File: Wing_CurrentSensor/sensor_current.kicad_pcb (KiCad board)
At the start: 2 copper layers, 50 x 50 mm, 18 parts, among them U1 TL084, U2 AD8226

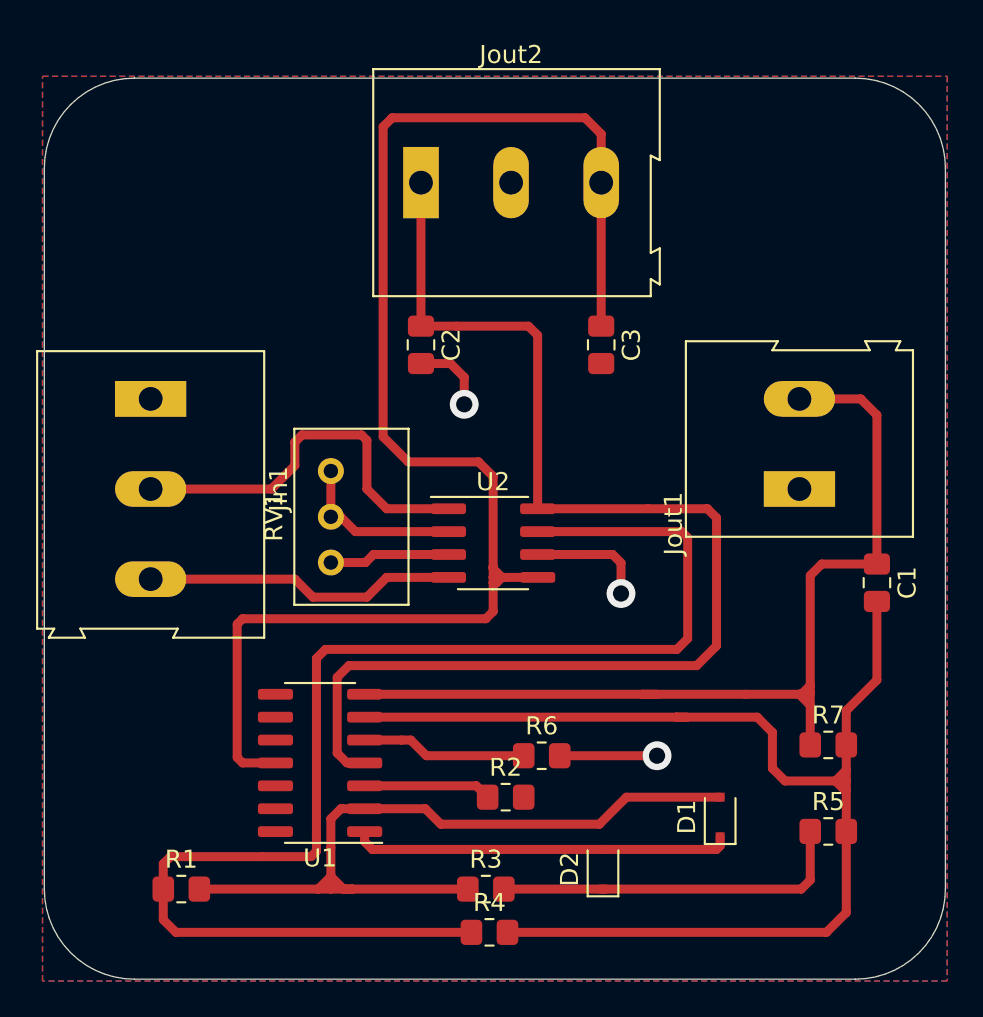
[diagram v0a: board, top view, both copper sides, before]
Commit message: AD8226 eliminated
auto_awesome
Se muestra la traducción de se reemplazo el AD8226 por un modulo del TL084, ademas se cambio el orden de los modulos, siendo estos el modulo B,C y D, se realizo nuevo esquematico y nueva PCB del circuito
Traducir se remplazo el AD8226 por un modulo del TL084, ademas se cambio el orden de los modulos, siendo estos el modulo B,C y D, se realizo nuevo esquematico y nueva PCB del circuito
174 / 5000
Resultados de traducción
The AD8226 was replaced by a TL084 module, also the order of the modules was changed, these being module B, C and D, a new schematic and new circuit PCB was made
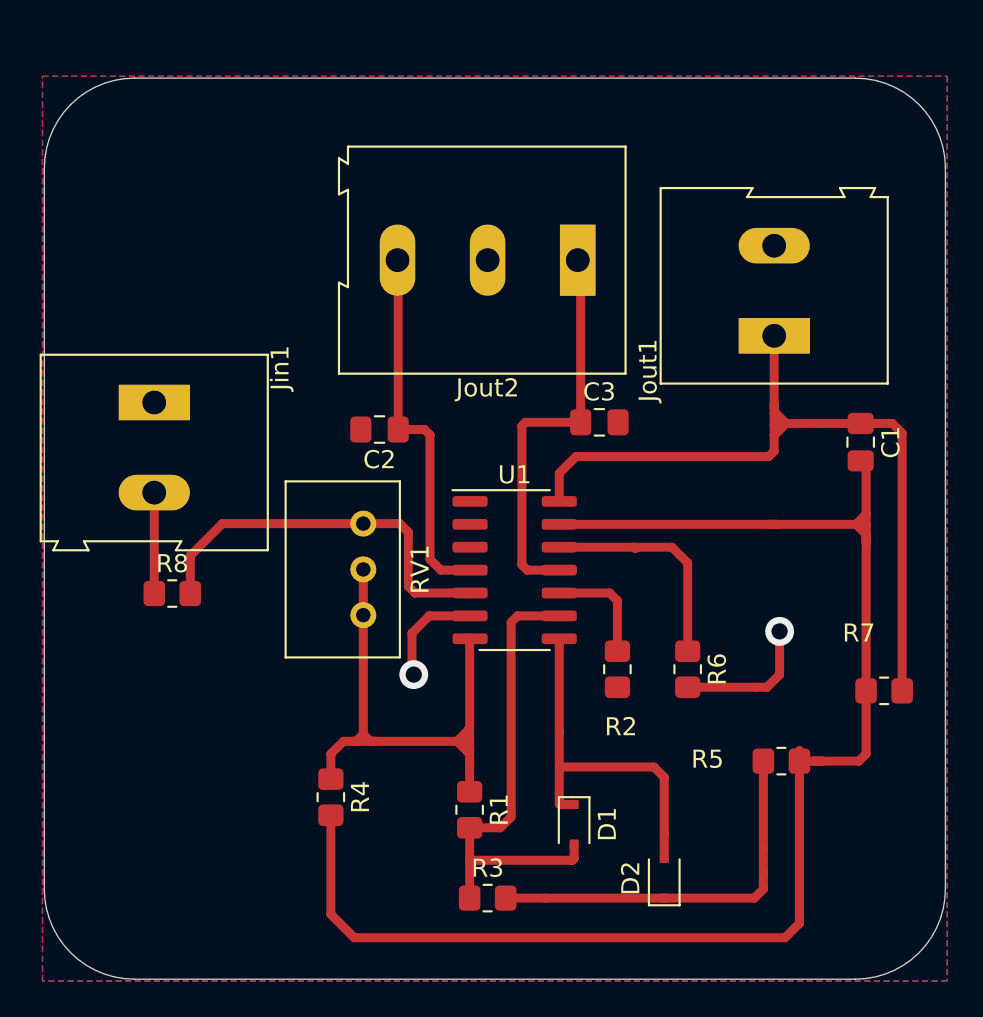
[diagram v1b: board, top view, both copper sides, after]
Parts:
- removed U2: AD8226, Package_SO:SOIC-8_3.9x4.9mm_P1.27mm
- added R8: 10K, Resistor_SMD:R_0805_2012Metric_Pad1.20x1.40mm_HandSolder, F.Cu at (48.1, 108.6)
- Jin1: value Screw_Terminal_01x03 -> Screw_Terminal_01x02; footprint TerminalBlock:TerminalBlock_Altech_AK300-3_P5.00mm -> TerminalBlock:TerminalBlock_Altech_AK300-2_P5.00mm
- moved R1 16.6 mm to (64.6, 120.6), turned to 270 degrees
- moved U1 15.2 mm to (67.1, 107.3), turned to 0 degrees
- moved R4 11.6 mm to (56.9, 119.9), turned to 270 degrees
- moved Jout2 9.70 mm to (70.6, 90.1), turned to 180 degrees
- moved R2 9.43 mm to (72.8, 112.8), turned to 270 degrees
- moved R6 9.42 mm to (76.7, 112.8), turned to 270 degrees
- moved Jout1 8.61 mm to (81.5, 94.3)
- moved RV1 8.20 mm to (58.7, 109.8), turned to 270 degrees
- moved D1 8.11 mm to (70.4, 121.4), turned to 270 degrees
- moved C1 7.85 mm to (86.3, 100.2)
- moved C2 5.23 mm to (59.6, 99.5), turned to 180 degrees
- moved R5 4.69 mm to (81.9, 117.9)
- moved R7 4.31 mm to (87.6, 114.0), turned to 180 degrees
- moved C3 4.30 mm to (71.8, 99.1), turned to 0 degrees
- moved D2 3.44 mm to (75.4, 124.4)
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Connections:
- Jin1 pad 2: /in- -> /in+
- Jout1 pad 1: GND -> /OUT
- Jout1 pad 2: /OUT -> GND
- Jout2 pad 1: /+Vs -> /-Vs
- Jout2 pad 3: /-Vs -> /+Vs
- RV1 pad 1: Net-(RV1-Pad1) -> /out1
- RV1 pad 2: Net-(RV1-Pad1) -> /out1
- RV1 pad 3: Net-(RV1-Pad3) -> Net-(R8-Pad2)
- U1 pad 1: Net-(D1-Pad1) -> (no net)
- U1 pad 10: (no net) -> Net-(R2-Pad1)
- U1 pad 12: (no net) -> Net-(R6-Pad1)
- U1 pad 13: (no net) -> Net-(C1-Pad2)
- U1 pad 14: (no net) -> /OUT
- U1 pad 2: Net-(D1-Pad2) -> (no net)
- U1 pad 3: Net-(R2-Pad1) -> (no net)
- U1 pad 5: Net-(R6-Pad1) -> Net-(R8-Pad2)
- U1 pad 6: Net-(C1-Pad2) -> GND
- U1 pad 7: /OUT -> /out1
- U1 pad 8: (no net) -> Net-(D1-Pad1)
- U1 pad 9: (no net) -> Net-(D1-Pad2)
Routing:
- net /-Vs: track 83.1 -> 22.4 mm
- net /+Vs: track 69.2 -> 20.8 mm
- net /out1: track 75.4 -> 32.3 mm
- net /in-: track 21.8 -> 0.00 mm
- net Net-(R8-Pad2): track 0.00 -> 21.8 mm
- net Net-(D1-Pad2): track 44.1 -> 26.7 mm
- net Net-(C1-Pad2): track 68.8 -> 82.3 mm
- net /in+: track 17.4 -> 5.60 mm
- net Net-(RV1-Pad1): track 9.41 -> 0.00 mm
- net /OUT: track 53.6 -> 44.2 mm
- net Net-(RV1-Pad3): track 6.71 -> 0.00 mm
- net GND: track 18.9 -> 13.8 mm, vias 3 -> 2
- net Net-(R6-Pad1): track 9.19 -> 12.5 mm
- net Net-(D2-Pad1): track 19.9 -> 21.6 mm
- net Net-(R2-Pad1): track 7.09 -> 6.25 mm

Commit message: Printable of PCB without AD8226
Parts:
- R8: value 10K -> 1K
